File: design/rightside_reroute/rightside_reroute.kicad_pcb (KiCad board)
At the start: 4 copper layers, 144 x 96.2 mm, 198 parts, among them IC1 BQ27441DRZT-G1A, IC2 XC9148G50CER-G, IC3 nRF52833-QDAA-R7, IC4 74AHCT125PW,118, IC5 MCP23018T-E_SS, IC6 XC9291B33D1R-G, J1 USB_C_Receptacle_USB2.0_16P, J2 Battery Pos, J3 Battery Neg, J4 OLED_128x32, J6 Conn_01x04, J7 F32Q-1A7H1-11012, U2 BQ24072RGT, U3 USB6B1, U5 PEC11L-4015F-S0015, U6 PEC11L-4015F-S0015, Y1 ECS-320-8-37B2-JTY-TR

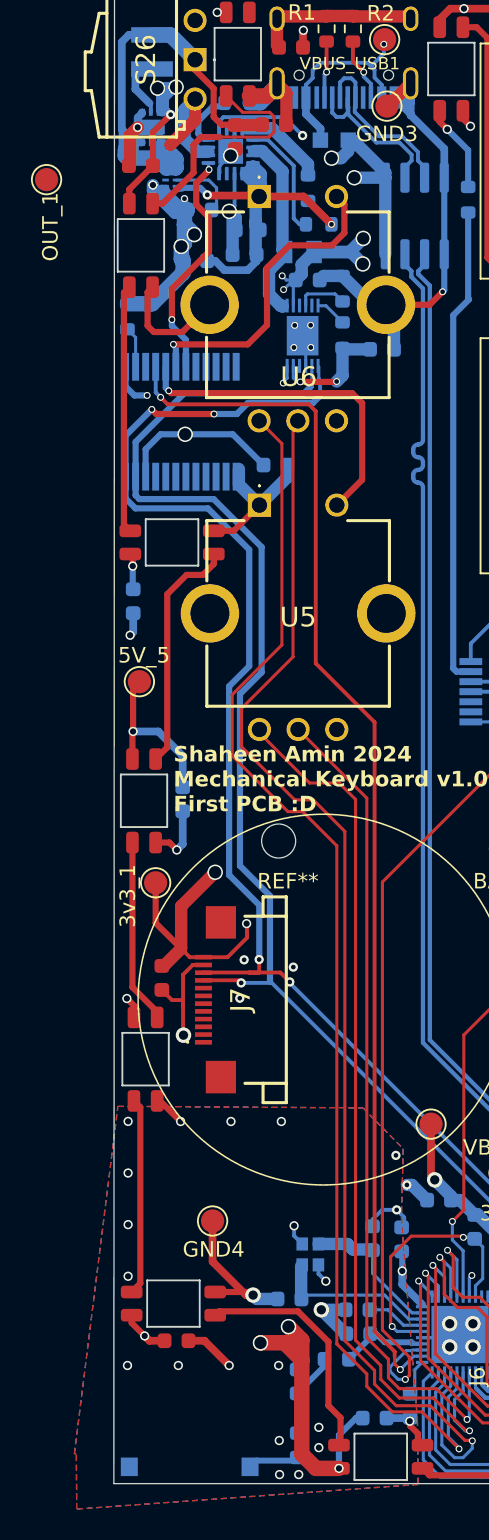
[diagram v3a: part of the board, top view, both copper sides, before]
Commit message: begin to move gpio expander
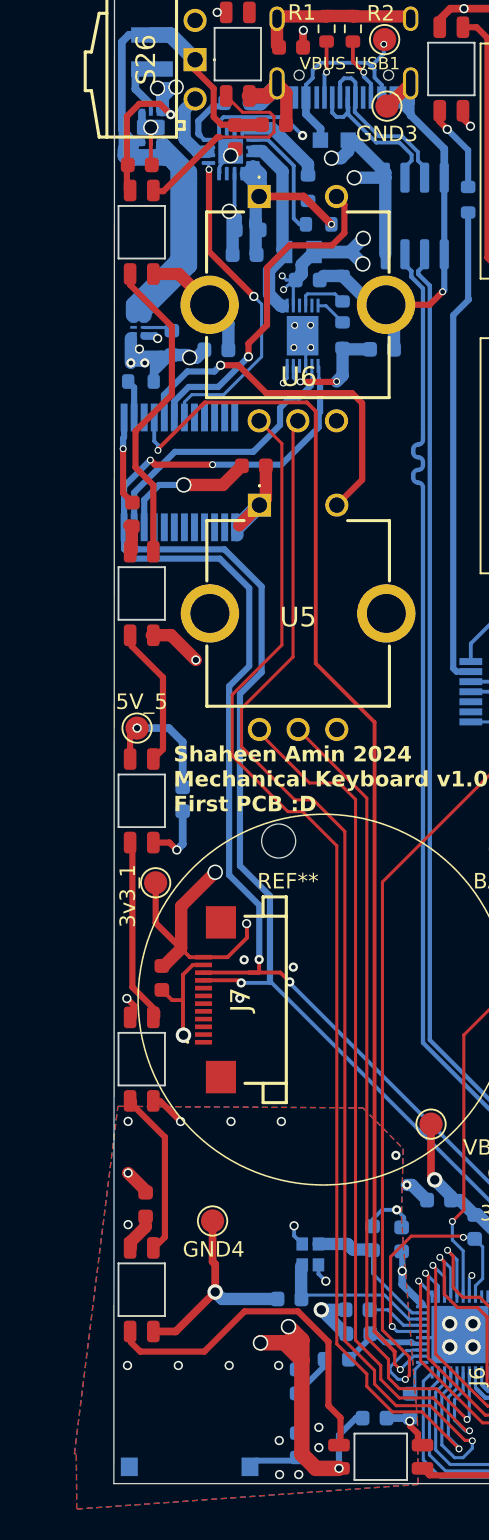
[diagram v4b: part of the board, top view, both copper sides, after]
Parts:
- removed OUT_1: TestPoint, TestPoint:TestPoint_Pad_D1.5mm
- C20, C46: moved to F.Cu
- moved IC6 9.74 mm to (93.2, 58.1)
- moved C39 9.02 mm to (93.6, 114.8), turned to 90 degrees
- moved L3 8.77 mm to (95.3, 59.1), turned to 90 degrees
- moved C13 5.91 mm to (98.2, 59.6)
- moved C46 5.60 mm to (92.8, 70.2), turned to -90 degrees
- moved R9 4.29 mm to (93.3, 61.6), turned to 0 degrees
- moved D46 3.84 mm to (93.4, 75.3), turned to 90 degrees
- moved IC5 3.28 mm to (95.8, 67.5)
- moved 5V_5 3.00 mm to (93.1, 84.0)
- moved D43 2.24 mm to (93.4, 120.3), turned to 90 degrees
- moved C20 1.40 mm to (100.6, 67.1)
- moved D47 0.85 mm to (93.4, 52.0)
- moved D44 0.25 mm to (93.4, 105.4)
- moved D45 0.15 mm to (93.4, 88.7)
- moved C27 0.09 mm to (93.2, 47.6), turned to 0 degrees
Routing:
- net Net-(IC2-BAT): track 36.1 -> 63.1 mm
- net Net-(D42-DOUT): track 15.3 -> 22.7 mm
- net Net-(D45-DOUT): track 15.4 -> 9.10 mm
- net /CHG: track 15.2 -> 21.1 mm
- net 3V3: track 82.0 -> 76.5 mm
- net Net-(D46-DOUT): track 16.1 -> 20.5 mm
- net /OUT: track 8.37 -> 4.75 mm
- net 5V: track 161.2 -> 158.5 mm, vias 56 -> 54
- net GND: track 293.7 -> 291.1 mm, vias 106 -> 105
- net Net-(IC6-LX): track 4.39 -> 1.88 mm
- net Net-(D43-DOUT): track 12.8 -> 10.6 mm
- net /INTA: track 78.5 -> 80.1 mm
- net Net-(D47-DOUT): track 16.1 -> 14.6 mm
- net /NO2: track 20.3 -> 21.8 mm
- net /NO: track 21.7 -> 22.8 mm
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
